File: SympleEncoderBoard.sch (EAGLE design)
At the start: 26 parts, among them IC1 STM32F446RET6, IC2 MCP2551-I_SN

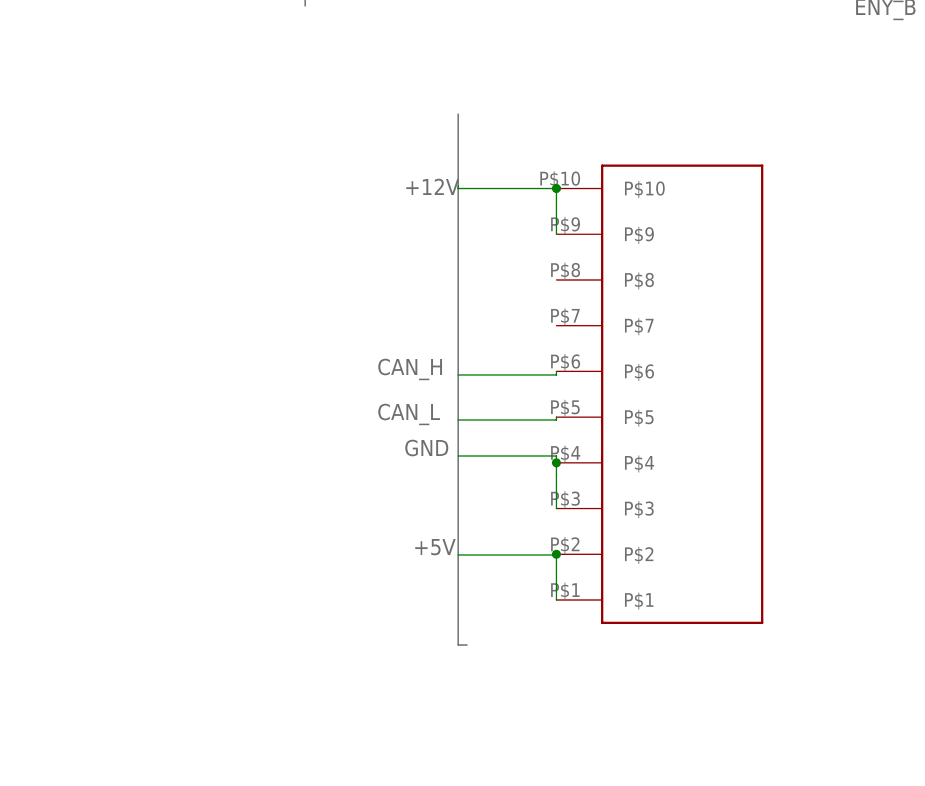
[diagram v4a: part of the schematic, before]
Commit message: 10pboxのピンアサイン間違えてました
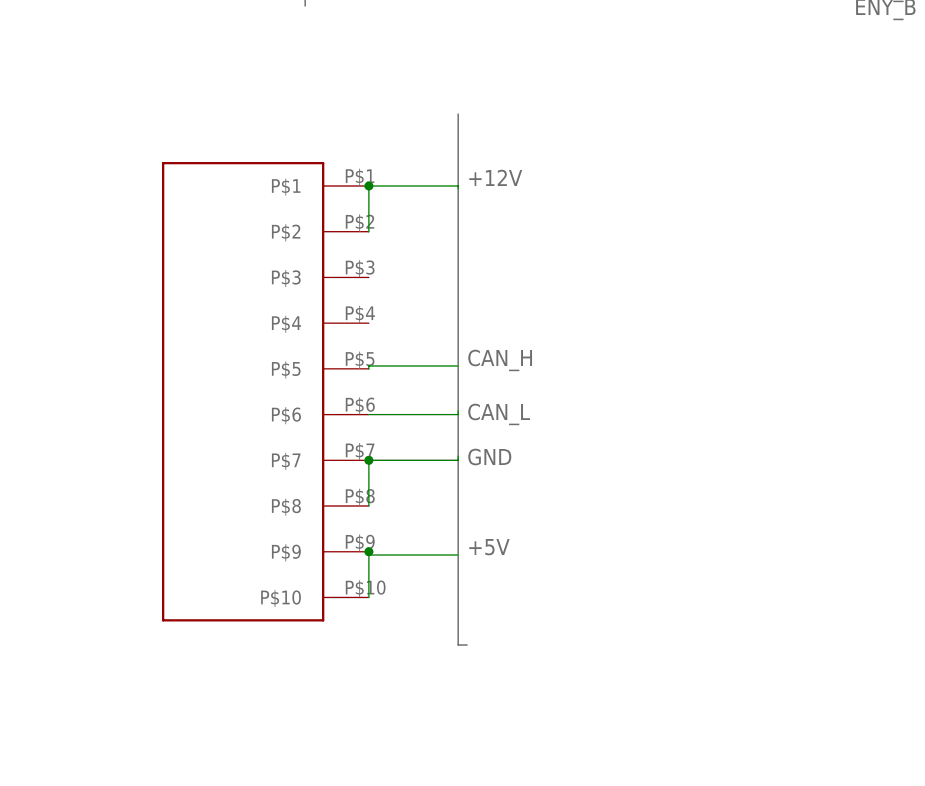
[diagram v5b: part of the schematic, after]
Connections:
- net +12V: now also BOX10P-L1.P$1, BOX10P-L1.P$2; no longer BOX10P-L1.P$10, BOX10P-L1.P$9
- net +5V: now also BOX10P-L1.P$10, BOX10P-L1.P$9; no longer BOX10P-L1.P$1, BOX10P-L1.P$2
- net CAN_H: now also BOX10P-L1.P$5; no longer BOX10P-L1.P$6
- net CAN_L: now also BOX10P-L1.P$6; no longer BOX10P-L1.P$5
- net GND: now also BOX10P-L1.P$7, BOX10P-L1.P$8; no longer BOX10P-L1.P$3, BOX10P-L1.P$4
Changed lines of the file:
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@@
 <attribute name="VALUE" x="-25.87" y="58.08" size="1.778" layer="96" align="center-left"/>
 </instance>
-<instance part="BOX10P-L1" gate="G$1" x="27" y="-30" smashed="yes" rot="R180"/>
+<instance part="BOX10P-L1" gate="G$1" x="-4" y="16" smashed="yes"/>
 <instance part="R2" gate="G$1" x="-14" y="53" smashed="yes">
 <attribute name="NAME" x="-17.81" y="54.4986" size="1.778" layer="95"/>
@@
 </segment>
 <segment>
-<pinref part="BOX10P-L1" gate="G$1" pin="P$4"/>
-<wire x1="11" y1="-14" x2="21.92" y2="-14" width="0.1524" layer="91"/>
-<wire x1="21.92" y1="-14" x2="21.92" y2="-14.76" width="0.1524" layer="91"/>
-<pinref part="BOX10P-L1" gate="G$1" pin="P$3"/>
-<wire x1="21.92" y1="-14.76" x2="21.92" y2="-19.84" width="0.1524" layer="91"/>
-<junction x="21.92" y="-14.76"/>
-<label x="5" y="-14" size="1.778" layer="95"/>
-</segment>
-<segment>
 <pinref part="R2" gate="G$1" pin="2"/>
 <wire x1="-8.92" y1="53" x2="-6" y2="53" width="0.1524" layer="91"/>
@@
 <label x="42" y="96" size="1.778" layer="95" rot="R90"/>
 </segment>
+<segment>
+<pinref part="BOX10P-L1" gate="G$1" pin="P$7"/>
+<wire x1="11" y1="-14" x2="11" y2="-14.48" width="0.1524" layer="91"/>
+<wire x1="11" y1="-14.48" x2="1.08" y2="-14.48" width="0.1524" layer="91"/>
+<pinref part="BOX10P-L1" gate="G$1" pin="P$8"/>
+<wire x1="1.08" y1="-14.48" x2="1.08" y2="-19.56" width="0.1524" layer="91"/>
+<junction x="1.08" y="-14.48"/>
+<label x="12" y="-15" size="1.778" layer="95"/>
+</segment>
 </net>
 <net name="NRST" class="0">
@@
 </segment>
 <segment>
-<pinref part="BOX10P-L1" gate="G$1" pin="P$1"/>
-<pinref part="BOX10P-L1" gate="G$1" pin="P$2"/>
-<wire x1="21.92" y1="-30" x2="21.92" y2="-24.92" width="0.1524" layer="91"/>
-<wire x1="11" y1="-25" x2="21.92" y2="-25" width="0.1524" layer="91"/>
-<wire x1="21.92" y1="-25" x2="21.92" y2="-24.92" width="0.1524" layer="91"/>
-<junction x="21.92" y="-24.92"/>
-<label x="6" y="-25" size="1.778" layer="95"/>
+<pinref part="BOX10P-L1" gate="G$1" pin="P$10"/>
+<pinref part="BOX10P-L1" gate="G$1" pin="P$9"/>
+<wire x1="1.08" y1="-29.72" x2="1.08" y2="-24.64" width="0.1524" layer="91"/>
+<wire x1="11" y1="-25" x2="1.08" y2="-25" width="0.1524" layer="91"/>
+<wire x1="1.08" y1="-25" x2="1.08" y2="-24.64" width="0.1524" layer="91"/>
+<junction x="1.08" y="-24.64"/>
+<label x="12" y="-25" size="1.778" layer="95"/>
 </segment>
 </net>
 <net name="CAN_L" class="0">
-<segment>
-<pinref part="BOX10P-L1" gate="G$1" pin="P$5"/>
-<wire x1="11" y1="-10" x2="21.92" y2="-10" width="0.1524" layer="91"/>
-<wire x1="21.92" y1="-10" x2="21.92" y2="-9.68" width="0.1524" layer="91"/>
-<label x="2" y="-10" size="1.778" layer="95"/>
-</segment>
 <segment>
 <pinref part="IC2" gate="G$1" pin="CANL"/>
@@
 <label x="-5" y="48" size="1.778" layer="95"/>
 </segment>
+<segment>
+<pinref part="BOX10P-L1" gate="G$1" pin="P$6"/>
+<wire x1="11" y1="-9" x2="11" y2="-9.4" width="0.1524" layer="91"/>
+<wire x1="11" y1="-9.4" x2="1.08" y2="-9.4" width="0.1524" layer="91"/>
+<label x="12" y="-10" size="1.778" layer="95"/>
+</segment>
 </net>
 <net name="CAN_H" class="0">
-<segment>
-<pinref part="BOX10P-L1" gate="G$1" pin="P$6"/>
-<wire x1="11" y1="-5" x2="21.92" y2="-5" width="0.1524" layer="91"/>
-<wire x1="21.92" y1="-5" x2="21.92" y2="-4.6" width="0.1524" layer="91"/>
-<label x="2" y="-5" size="1.778" layer="95"/>
-</segment>
 <segment>
 <pinref part="IC2" gate="G$1" pin="CANH"/>
@@
 <label x="-5" y="50" size="1.778" layer="95"/>
 </segment>
+<segment>
+<pinref part="BOX10P-L1" gate="G$1" pin="P$5"/>
+<wire x1="11" y1="-4" x2="1.08" y2="-4" width="0.1524" layer="91"/>
+<wire x1="1.08" y1="-4" x2="1.08" y2="-4.32" width="0.1524" layer="91"/>
+<label x="12" y="-4" size="1.778" layer="95"/>
+</segment>
 </net>
 <net name="N$7" class="0">
@@
 <net name="+12V" class="0">
 <segment>
-<pinref part="BOX10P-L1" gate="G$1" pin="P$10"/>
-<wire x1="21.92" y1="15.72" x2="11" y2="15.72" width="0.1524" layer="91"/>
 <wire x1="11" y1="15.72" x2="11" y2="16" width="0.1524" layer="91"/>
-<pinref part="BOX10P-L1" gate="G$1" pin="P$9"/>
-<wire x1="21.92" y1="15.72" x2="21.92" y2="10.64" width="0.1524" layer="91"/>
-<junction x="21.92" y="15.72"/>
-<label x="5" y="15" size="1.778" layer="95"/>
 </segment>
 <segment>
@@
 <label x="39" y="95" size="1.778" layer="95" rot="R90"/>
 </segment>
-</net>
+<segment>
+<pinref part="BOX10P-L1" gate="G$1" pin="P$1"/>
+<pinref part="BOX10P-L1" gate="G$1" pin="P$2"/>
+<wire x1="1.08" y1="16" x2="1.08" y2="10.92" width="0.1524" layer="91"/>
+<wire x1="11" y1="16" x2="1.08" y2="16" width="0.1524" layer="91"/>
+<junction x="1.08" y="16"/>
+<label x="12" y="16" size="1.778" layer="95"/>
+</segment>
+</net>

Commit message: CANトランシーバの位置と型番更新、MLCC・VDD・VSS接続、配線太さ、14Pコネクタ配置変更
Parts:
- removed IC2: MCP2551-I_SN, MCP2551-I_SN:MCP2551-I_SN
- added C4: 0.1μ, rcl:C-EUC1608
- added C5, C6, C7: 0.1μ, rcl:C-EUC0603
- added R4: 120, rcl:R-US_R0603
- added U$3: MCP2562MCP2561-SN, user_ic:MCP2562MCP2561-SN
- C1: value (none) -> 1μ
- R2: value 33k -> 10k
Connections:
- net +3.3V: now also C5.1, C6.1, C7.1, IC1.VDD_2, IC1.VDD_3, IC1.VDD_4, U$3.VIO
- net +5V: now also C4.1, R2.2, U$3.VDD; no longer IC2.VDD
- net CAN_H: now also R4.2, U$3.CANH; no longer IC2.CANH
- net CAN_L: now also R4.1, U$3.CANL; no longer IC2.CANL
- net CAN_RX: now also U$3.RXD; no longer IC2.RXD
- net CAN_TX: now also U$3.TXD; no longer IC2.TXD
- net GND: now also C4.2, C5.2, C6.2, C7.2, U$3.VSS; no longer IC2.VSS, R2.2
- net N$7: now also U$3.STBY; no longer IC2.RS
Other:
- moved on the sheet: R2

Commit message: GYRO用XHコネクタを横から縦に、テキストの文字を少し拡大、ベタパターンDRCチェック済
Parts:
- GYRO: value S4B-XH-A_LF__SN_ -> B4B-XH-A_LF__SN_; device S4B-XH-A_LF__SN_:S4B-XH-A_LF__SN_ -> B4B-XH-A_LF__SN_:B4B-XH-A_LF__SN_
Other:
- moved on the sheet: GYRO
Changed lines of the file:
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@@
 <part name="ENCODER_X" library="S4B-XH-A_LF__SN_" deviceset="S4B-XH-A_LF__SN_" device=""/>
 <part name="ENCODER_Y" library="S4B-XH-A_LF__SN_" deviceset="S4B-XH-A_LF__SN_" device=""/>
-<part name="GYRO" library="S4B-XH-A_LF__SN_" deviceset="S4B-XH-A_LF__SN_" device=""/>
 <part name="BOX10P-L1" library="user_conector" deviceset="BOX10P" device="BOX10P-L"/>
 <part name="U$2" library="SympleEncoderBoard" deviceset="BP5293-33" device=""/>
@@
 <part name="C6" library="rcl" library_urn="urn:adsk.eagle:library:334" deviceset="C-EU" device="C0603" package3d_urn="urn:adsk.eagle:package:23616/2" value="0.1μ"/>
 <part name="C7" library="rcl" library_urn="urn:adsk.eagle:library:334" deviceset="C-EU" device="C0603" package3d_urn="urn:adsk.eagle:package:23616/2" value="0.1μ"/>
+<part name="GYRO" library="B4B-XH-A_LF__SN_" deviceset="B4B-XH-A_LF__SN_" device=""/>
 </parts>
 <sheets>
@@
 <attribute name="VALUE" x="223.51" y="-5.92" size="1.778" layer="96" align="center-left"/>
 </instance>
-<instance part="GYRO" gate="G$1" x="207" y="-33" smashed="yes">
-<attribute name="NAME" x="223.51" y="-25.38" size="1.778" layer="95" align="center-left"/>
-<attribute name="VALUE" x="223.51" y="-27.92" size="1.778" layer="96" align="center-left"/>
-</instance>
 <instance part="BOX10P-L1" gate="G$1" x="-4" y="16" smashed="yes"/>
 <instance part="U$2" gate="G$1" x="41.18" y="133.46" smashed="yes"/>
@@
 <attribute name="NAME" x="138.524" y="11.381" size="1.778" layer="95"/>
 <attribute name="VALUE" x="138.524" y="6.301" size="1.778" layer="96"/>
+</instance>
+<instance part="GYRO" gate="G$1" x="207" y="-51" smashed="yes">
+<attribute name="NAME" x="223.51" y="-43.38" size="1.778" layer="95" align="center-left"/>
+<attribute name="VALUE" x="223.51" y="-45.92" size="1.778" layer="96" align="center-left"/>
 </instance>
 </instances>
@@
 </segment>
 <segment>
-<pinref part="GYRO" gate="G$1" pin="1"/>
-<wire x1="207" y1="-33" x2="200" y2="-33" width="0.1524" layer="91"/>
-<label x="194" y="-33" size="1.778" layer="95"/>
-</segment>
-<segment>
 <pinref part="U$2" gate="G$1" pin="GND"/>
 <wire x1="41.18" y1="123.46" x2="41.18" y2="102" width="0.1524" layer="91"/>
@@
 <label x="137" y="-5" size="1.778" layer="95" rot="R90"/>
 </segment>
+<segment>
+<pinref part="GYRO" gate="G$1" pin="1"/>
+<wire x1="207" y1="-51" x2="200" y2="-51" width="0.1524" layer="91"/>
+<label x="194" y="-51" size="1.778" layer="95"/>
+</segment>
 </net>
 <net name="NRST" class="0">
@@
 <segment>
 <pinref part="GYRO" gate="G$1" pin="3"/>
-<wire x1="207" y1="-38.08" x2="207" y2="-38" width="0.1524" layer="91"/>
-<wire x1="207" y1="-38" x2="200" y2="-38" width="0.1524" layer="91"/>
-<label x="189" y="-38" size="1.778" layer="95"/>
+<wire x1="207" y1="-56.08" x2="200" y2="-56.08" width="0.1524" layer="91"/>
+<wire x1="200" y1="-56.08" x2="200" y2="-56" width="0.1524" layer="91"/>
+<label x="189" y="-56" size="1.778" layer="95"/>
 </segment>
 </net>
@@
 <segment>
 <pinref part="GYRO" gate="G$1" pin="2"/>
-<wire x1="207" y1="-35.54" x2="200" y2="-35.54" width="0.1524" layer="91"/>
-<wire x1="200" y1="-35.54" x2="200" y2="-36" width="0.1524" layer="91"/>
-<label x="189" y="-36" size="1.778" layer="95"/>
+<wire x1="207" y1="-53.54" x2="200" y2="-53.54" width="0.1524" layer="91"/>
+<wire x1="200" y1="-53.54" x2="200" y2="-54" width="0.1524" layer="91"/>
+<label x="189" y="-54" size="1.778" layer="95"/>
 </segment>
 </net>
@@
 <wire x1="200" y1="-18.62" x2="200" y2="-19" width="0.1524" layer="91"/>
 <label x="195" y="-19" size="1.778" layer="95"/>
-</segment>
-<segment>
-<pinref part="GYRO" gate="G$1" pin="4"/>
-<wire x1="207" y1="-40.62" x2="200" y2="-40.62" width="0.1524" layer="91"/>
-<wire x1="200" y1="-40.62" x2="200" y2="-41" width="0.1524" layer="91"/>
-<label x="195" y="-41" size="1.778" layer="95"/>
 </segment>
 <segment>
@@
 <label x="-5" y="53" size="1.778" layer="95"/>
 </segment>
-</net>
+<segment>
+<pinref part="GYRO" gate="G$1" pin="4"/>
+<wire x1="207" y1="-58.62" x2="200" y2="-58.62" width="0.1524" layer="91"/>
+<wire x1="200" y1="-58.62" x2="200" y2="-59" width="0.1524" layer="91"/>
+<label x="195" y="-59" size="1.778" layer="95"/>
+</segment>
+</net>

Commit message: エラー等修正しました。
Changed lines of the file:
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@@
 <setting verticaltext="up"/>
 </settings>
-<grid distance="1" unitdist="mm" unit="mm" style="lines" multiple="1" display="yes" altdistance="0.25" altunitdist="mm" altunit="mm"/>
+<grid distance="1" unitdist="mm" unit="mm" style="lines" multiple="1" display="yes" altdistance="0.1" altunitdist="mm" altunit="mm"/>
 <layers>
 <layer number="1" name="Top" color="4" fill="1" visible="no" active="no"/>
@@
 </segment>
 <segment>
-<wire x1="129.54" y1="1" x2="130" y2="1" width="0.1524" layer="91"/>
-</segment>
-<segment>
-<pinref part="IC1" gate="G$1" pin="VSS_2"/>
-<wire x1="129.54" y1="15.24" x2="129.54" y2="1" width="0.1524" layer="91"/>
-<wire x1="129.54" y1="1" x2="130" y2="1" width="0.1524" layer="91"/>
-<label x="130" y="-5" size="1.778" layer="95" rot="R90"/>
-</segment>
-<segment>
-<pinref part="C2" gate="G$1" pin="2"/>
-<wire x1="127" y1="6.92" x2="127" y2="1" width="0.1524" layer="91"/>
-<wire x1="127" y1="1" x2="128" y2="1" width="0.1524" layer="91"/>
-<label x="128" y="-5" size="1.778" layer="95" rot="R90"/>
-</segment>
-<segment>
 <pinref part="C3" gate="G$1" pin="2"/>
 <wire x1="95" y1="2.92" x2="95" y2="1" width="0.1524" layer="91"/>
@@
 <wire x1="164" y1="-22.62" x2="163.62" y2="-22.62" width="0.1524" layer="91"/>
 <junction x="163.62" y="-22.62"/>
-<label x="164" y="-36" size="1.778" layer="95" rot="R90"/>
+<label x="165" y="-36" size="1.778" layer="95" rot="R90"/>
 </segment>
 <segment>
@@
 <label x="194" y="-51" size="1.778" layer="95"/>
 </segment>
+<segment>
+<pinref part="C2" gate="G$1" pin="2"/>
+<wire x1="127" y1="6.92" x2="127" y2="1" width="0.1524" layer="91"/>
+<label x="127" y="-5" size="1.778" layer="95" rot="R90"/>
+</segment>
+<segment>
+<pinref part="IC1" gate="G$1" pin="VSS_2"/>
+<wire x1="129.54" y1="15.24" x2="129.54" y2="1" width="0.1524" layer="91"/>
+<wire x1="129.54" y1="1" x2="129.5" y2="1" width="0.1524" layer="91"/>
+<label x="130" y="-5" size="1.778" layer="95" rot="R90"/>
+</segment>
 </net>
